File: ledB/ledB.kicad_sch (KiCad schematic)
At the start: 9 parts, among them U1 OPAMP, Y1 Piezo Crystal

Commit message: hmem-made2
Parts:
- removed U1: OPAMP, Package_DIP:DIP-8_W7.62mm, symbol Amplifier_Operational:LM741
- added D3: LED, LED_THT:LED_D3.0mm, symbol Device:LED
- added U1: LMV321, Package_TO_SOT_SMD:SOT-23-5_HandSoldering, symbol Amplifier_Operational:LMV321
- BT1: footprint 1_my_custom_lib:BAT_BH800S -> Connector_Wire:SolderWire-2.5sqmm_1x02_P7.2mm_D2.4mm_OD3.6mm
- R1, R2, R3, R4: footprint Resistor_THT:R_Axial_DIN0207_L6.3mm_D2.5mm_P10.16mm_Horizontal -> Resistor_SMD:R_0805_2012Metric
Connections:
- net GND: now also U1.2 (V-)
- net VCC: now also D3.2 (A), U1.5 (V+)
- net at R1.1, R3.2: now also U1.1 (+)
- net at R2.1, R4.1: now also U1.4
- net at D1.2 (A), R4.2: now also D3.1 (K)
- net at R2.2, Y1.2: now also U1.3 (-)
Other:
- note added: "(optional) go on output as well just reversed to pickup the reversed volt from piezo"
- note added: "all resistors same value (higher then 1M) we use a Rail to Rail CMOS (LMV358 MCP6001 TLC271 LMV321) R4 - optional current limit resistor important if adding LDR distrotion will be much better if running above 3v, we will need to adjust the volt devider R3 volt of pin3 must be lower then 2v (led opens) limitations: BLUE led will possibly not work with the resistor lithium recommded for high volt L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"
- note removed: "optional current limit resistor important if adding LDR distrotion will be much better all resistors, same value (higher then 1M) if we use a Rail to Rail CMOS (LMV358 MCP6001 TLC271 LMV321) if running above 3v, wewill need to adjust the volt devider R3 volt of pin3 must be lower then 2v (led opens) limitations: BLUE led will possibly not work with the ressitor lithium recommded for high volt LEDs"
- moved on the sheet: D1

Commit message: sent to fab
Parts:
- added H1: MountingHole, MountingHole:MountingHole_3.5mm, symbol Mechanical:MountingHole
- added TP1: TestPoint, TestPoint:TestPoint_Pad_2.0x2.0mm, symbol Connector:TestPoint
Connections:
- net at R2.1, R4.1, U1.4: now also TP1.1
- net piezo+: now reaches R2.2, U1.3 (-), Y1.2

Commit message: v2 based on ledman
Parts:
- removed D3: LED, LED_THT:LED_D3.0mm, symbol Device:LED
- removed TP1: TestPoint, TestPoint:TestPoint_Pad_2.0x2.0mm, symbol Connector:TestPoint
- added C1: 47n, Capacitor_SMD:C_0805_2012Metric, symbol Device:C
- R1: value 10M -> 2M2
- R2, R3: value 10M -> 3M3
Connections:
- net GND: now also C1.2
- net at R1.1, R3.2, U1.1 (+): now also C1.1
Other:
- note removed: "(optional) go on output as well just reversed to pickup the reversed volt from piezo"
- moved on the sheet: R2

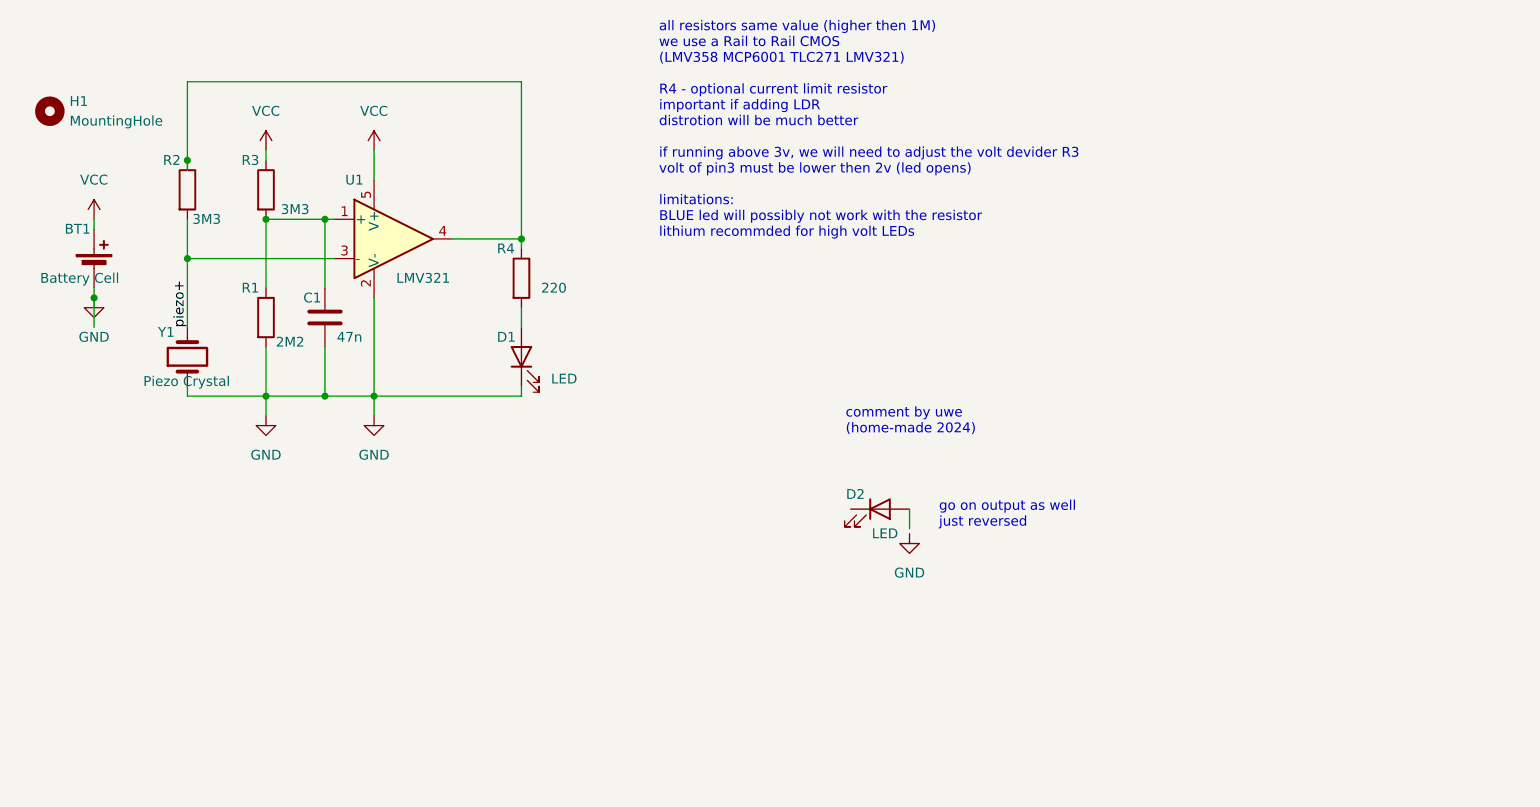
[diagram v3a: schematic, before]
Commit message: fit schema to wue site
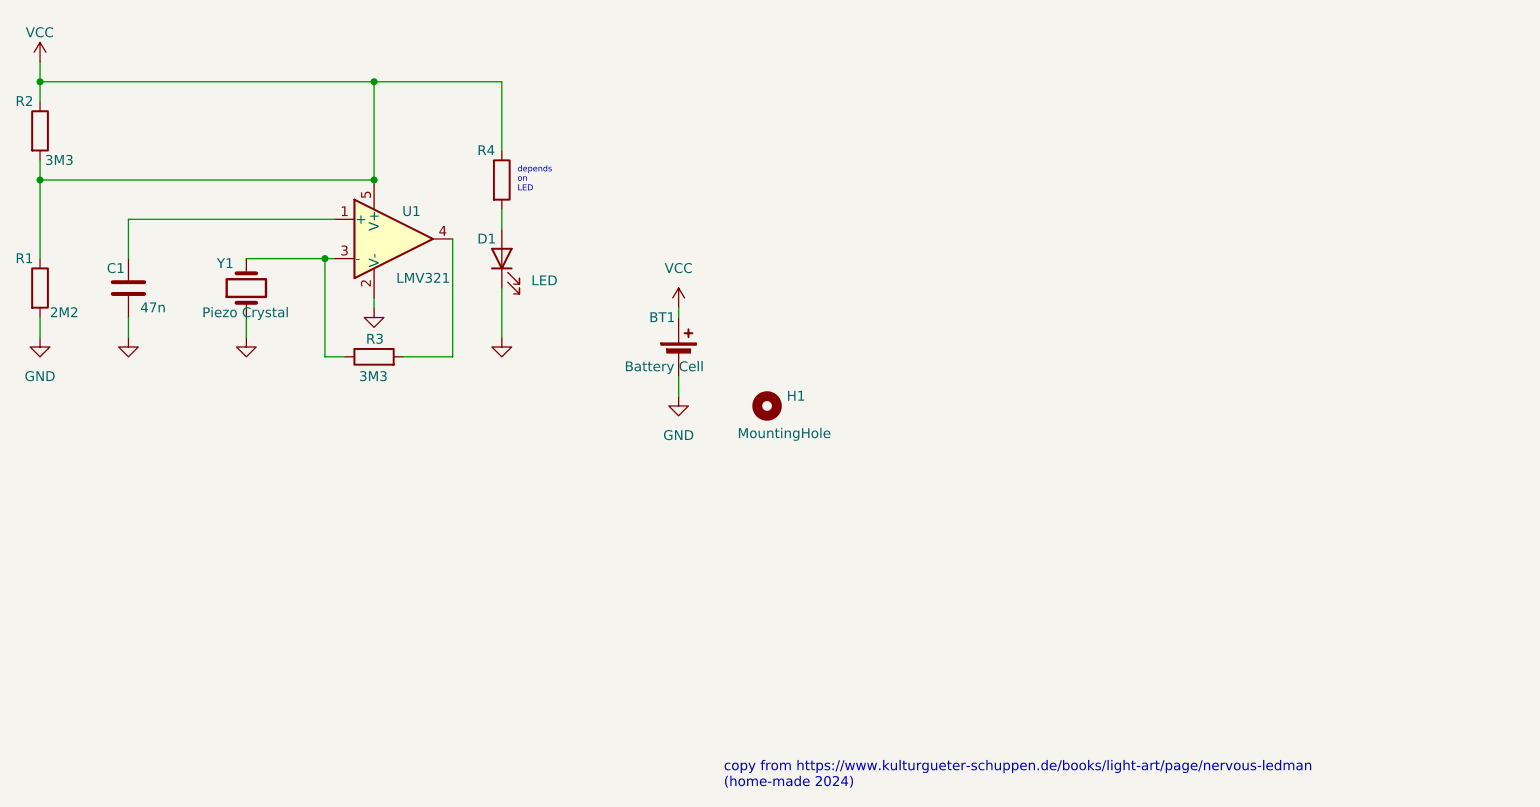
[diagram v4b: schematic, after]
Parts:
- removed D2: LED, LED_THT:LED_D3.0mm, symbol Device:LED
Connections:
- net VCC: now also R1.1, R2.1, R2.2, R4.1; no longer R3.1
- net at C1.1, U1.1 (+): no longer R1.1, R3.2
- net piezo+: no longer names the net of U1.3 (-), Y1.2
- net piezo+: now also R3.1; no longer R2.2
- new net: R3.2, U1.4
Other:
- note added: "copy from https://www.kulturgueter-schuppen.de/books/light-art/page/nervous-ledman (home-made 2024)"
- note added: "depends on LED"
- note removed: "all resistors same value (higher then 1M) we use a Rail to Rail CMOS (LMV358 MCP6001 TLC271 LMV321) R4 - optional current limit resistor important if adding LDR distrotion will be much better if running above 3v, we will need to adjust the volt devider R3 volt of pin3 must be lower then 2v (led opens) limitations: BLUE led will possibly not work with the resistor lithium recommded for high volt L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"
- note removed: "comment by uwe (home-made 2024)"
- note removed: "go on output as well just reversed"
- moved on the sheet: BT1, C1, D1, H1, R1, R2, R3, R4, Y1
